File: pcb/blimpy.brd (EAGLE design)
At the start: 250 x 167 mm, 76 parts, among them J1 MICRO-USB, J4 3-PIN SMD, J5 3-PIN SMD, J6 3-PIN SMD, J7 3-PIN SMD, Q1 mmbt2222, Q2 mmbt2222, Q3 DMG3415U, U1 RGB, U10 MAX17048, U2 AP2112-3.3, U3 MCP73831T-2, U4 BNO080, U5 SX1509, U6 SX1509, U7 CP2104, U9 ESP-WROOM-32

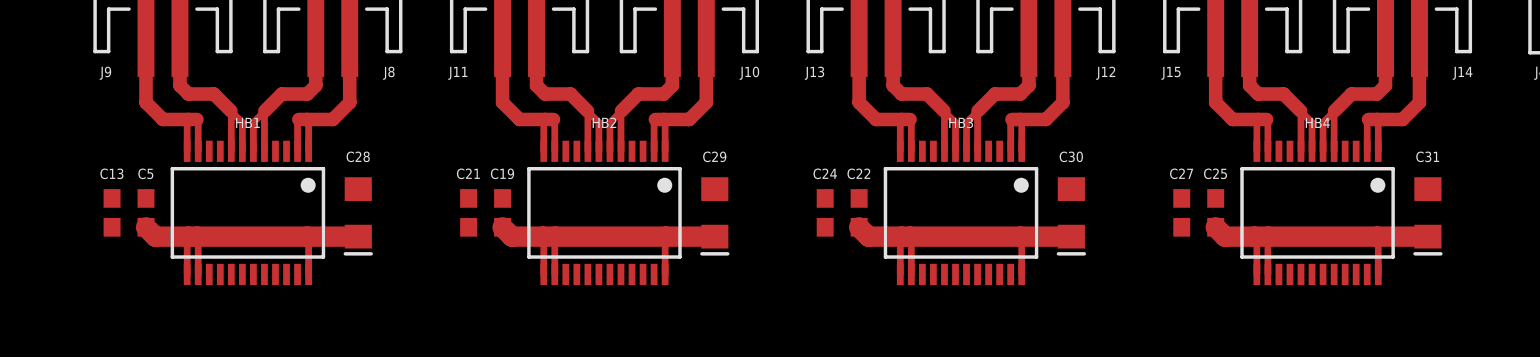
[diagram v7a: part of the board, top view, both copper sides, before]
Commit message: added hbridge gnd  traces
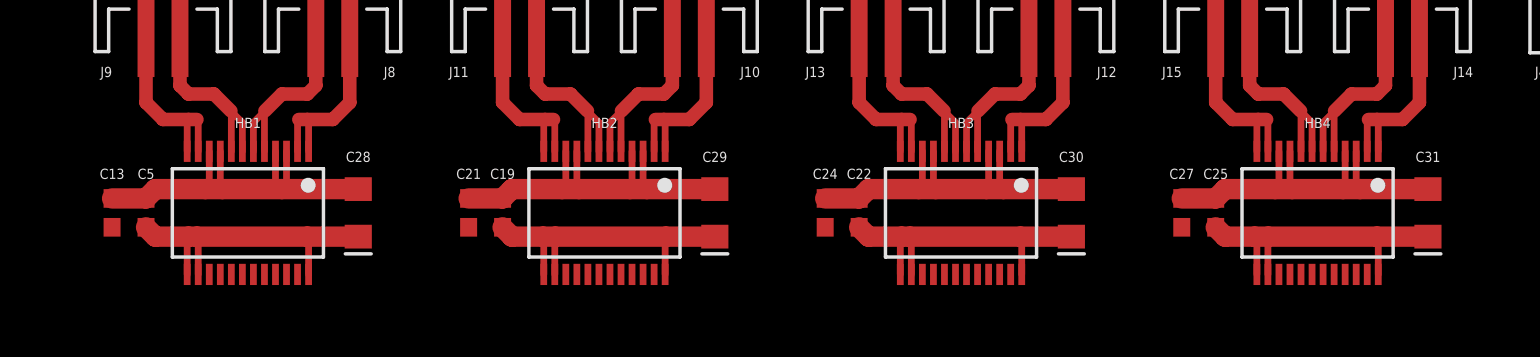
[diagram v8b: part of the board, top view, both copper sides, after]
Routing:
- net GND: track 0.00 -> 95.8 mm
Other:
- board text added: "Trace Widths for 1oz Copper: Logic: 0.4mm, 15mil (1A) Actors: 0.8mm, 30mil (2A) HBridge: 1.2mm, 45mil (3A) Battery: 1.6mm, 60mil (4A) Text Sizes Vector, 0.6, 15%"
- board text removed: "Trace Widths for 1oz Copper: Logic: 0.4mm, 15mil Actors: 0.8mm, 30mil (2A) Battery: 1.6mm, 60mil (4A) Text Sizes Vector, 0.6, 15%"
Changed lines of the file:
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@@
 <text x="225" y="75.5" size="0.6" layer="25" font="vector" ratio="15" align="bottom-center">U1</text>
 <text x="7" y="170.5" size="1.778" layer="51">Trace Widths for 1oz Copper:
-Logic: 0.4mm, 15mil
+Logic: 0.4mm, 15mil (1A)
 Actors: 0.8mm, 30mil (2A)
+HBridge: 1.2mm, 45mil (3A)
 Battery: 1.6mm, 60mil (4A)
 Text Sizes
@@
 <contactref element="U10" pad="P$9"/>
 <contactref element="C11" pad="2"/>
-<wire x1="106.125" y1="147.125" x2="106.775" y2="147.125" width="0" layer="19" extent="1-1"/>
-<wire x1="102.875" y1="147.125" x2="106.125" y2="147.125" width="0" layer="19" extent="1-1"/>
-<wire x1="102.225" y1="147.125" x2="102.875" y2="147.125" width="0" layer="19" extent="1-1"/>
-<wire x1="98.5" y1="144.35" x2="102.225" y2="147.125" width="0" layer="19" extent="1-1"/>
-<wire x1="96.5" y1="144.35" x2="98.5" y2="144.35" width="0" layer="19" extent="1-1"/>
-<wire x1="111" y1="144.9" x2="106.775" y2="147.125" width="0" layer="19" extent="1-1"/>
+<wire x1="48" y1="144.9" x2="43.5" y2="144.9" width="1.2" layer="1"/>
+<wire x1="43.5" y1="144.9" x2="40" y2="144.9" width="1.2" layer="1"/>
+<wire x1="40" y1="144.9" x2="39" y2="144.9" width="1.2" layer="1"/>
+<wire x1="39" y1="144.9" x2="36.05" y2="144.9" width="1.2" layer="1"/>
+<wire x1="36.05" y1="144.9" x2="35.5" y2="144.35" width="1.2" layer="1"/>
+<wire x1="33.5" y1="144.35" x2="35.5" y2="144.35" width="1.2" layer="1"/>
+<wire x1="69" y1="144.9" x2="65" y2="144.9" width="1.2" layer="1"/>
+<wire x1="65" y1="144.9" x2="64" y2="144.9" width="1.2" layer="1"/>
+<wire x1="64" y1="144.9" x2="61" y2="144.9" width="1.2" layer="1"/>
+<wire x1="61" y1="144.9" x2="60" y2="144.9" width="1.2" layer="1"/>
+<wire x1="60" y1="144.9" x2="57.05" y2="144.9" width="1.2" layer="1"/>
+<wire x1="57.05" y1="144.9" x2="56.5" y2="144.35" width="1.2" layer="1"/>
+<wire x1="56.5" y1="144.35" x2="54.5" y2="144.35" width="1.2" layer="1"/>
+<wire x1="90" y1="144.9" x2="86" y2="144.9" width="1.2" layer="1"/>
+<wire x1="86" y1="144.9" x2="85" y2="144.9" width="1.2" layer="1"/>
+<wire x1="85" y1="144.9" x2="82" y2="144.9" width="1.2" layer="1"/>
+<wire x1="82" y1="144.9" x2="81" y2="144.9" width="1.2" layer="1"/>
+<wire x1="81" y1="144.9" x2="78.05" y2="144.9" width="1.2" layer="1"/>
+<wire x1="78.05" y1="144.9" x2="77.5" y2="144.35" width="1.2" layer="1"/>
+<wire x1="77.5" y1="144.35" x2="75.5" y2="144.35" width="1.2" layer="1"/>
+<wire x1="111" y1="144.9" x2="107" y2="144.9" width="1.2" layer="1"/>
+<wire x1="107" y1="144.9" x2="106" y2="144.9" width="1.2" layer="1"/>
+<wire x1="106" y1="144.9" x2="103" y2="144.9" width="1.2" layer="1"/>
+<wire x1="103" y1="144.9" x2="102" y2="144.9" width="1.2" layer="1"/>
+<wire x1="102" y1="144.9" x2="99.05" y2="144.9" width="1.2" layer="1"/>
+<wire x1="99.05" y1="144.9" x2="98.5" y2="144.35" width="1.2" layer="1"/>
+<wire x1="98.5" y1="144.35" x2="96.5" y2="144.35" width="1.2" layer="1"/>
+<wire x1="106.775" y1="147.125" x2="106.775" y2="145.125" width="0.4" layer="1"/>
+<wire x1="106.775" y1="145.125" x2="107" y2="144.9" width="0.4" layer="1"/>
+<wire x1="106.125" y1="147.125" x2="106.125" y2="145.025" width="0.4" layer="1"/>
+<wire x1="106.125" y1="145.025" x2="106" y2="144.9" width="0.4" layer="1"/>
+<wire x1="102.875" y1="147.125" x2="102.875" y2="145.025" width="0.4" layer="1"/>
+<wire x1="102.875" y1="145.025" x2="103" y2="144.9" width="0.4" layer="1"/>
+<wire x1="102.225" y1="147.125" x2="102.225" y2="145.125" width="0.4" layer="1"/>
+<wire x1="102.225" y1="145.125" x2="102" y2="144.9" width="0.4" layer="1"/>
+<wire x1="85.125" y1="147.125" x2="85.125" y2="145.025" width="0.4" layer="1"/>
+<wire x1="85.125" y1="145.025" x2="85" y2="144.9" width="0.4" layer="1"/>
+<wire x1="85.775" y1="147.125" x2="85.775" y2="145.125" width="0.4" layer="1"/>
+<wire x1="85.775" y1="145.125" x2="86" y2="144.9" width="0.4" layer="1"/>
+<wire x1="81.875" y1="147.125" x2="81.875" y2="145.025" width="0.4" layer="1"/>
+<wire x1="81.875" y1="145.025" x2="82" y2="144.9" width="0.4" layer="1"/>
+<wire x1="81.225" y1="147.125" x2="81.225" y2="145.125" width="0.4" layer="1"/>
+<wire x1="81.225" y1="145.125" x2="81" y2="144.9" width="0.4" layer="1"/>
+<wire x1="64.775" y1="147.125" x2="64.775" y2="145.125" width="0.4" layer="1"/>
+<wire x1="64.775" y1="145.125" x2="65" y2="144.9" width="0.4" layer="1"/>
+<wire x1="64.125" y1="147.125" x2="64.125" y2="145.025" width="0.4" layer="1"/>
+<wire x1="64.125" y1="145.025" x2="64" y2="144.9" width="0.4" layer="1"/>
+<wire x1="60.875" y1="147.125" x2="60.875" y2="145.025" width="0.4" layer="1"/>
+<wire x1="60.875" y1="145.025" x2="61" y2="144.9" width="0.4" layer="1"/>
+<wire x1="60.225" y1="147.125" x2="60.225" y2="145.125" width="0.4" layer="1"/>
+<wire x1="60.225" y1="145.125" x2="60" y2="144.9" width="0.4" layer="1"/>
+<wire x1="43.775" y1="147.125" x2="43.775" y2="145.175" width="0.4" layer="1"/>
+<wire x1="43.775" y1="145.175" x2="43.5" y2="144.9" width="0.4" layer="1"/>
+<wire x1="43.125" y1="147.125" x2="43.125" y2="145.275" width="0.4" layer="1"/>
+<wire x1="43.125" y1="145.275" x2="43.5" y2="144.9" width="0.4" layer="1"/>
+<wire x1="39.875" y1="147.125" x2="39.875" y2="145.025" width="0.4" layer="1"/>
+<wire x1="39.875" y1="145.025" x2="40" y2="144.9" width="0.4" layer="1"/>
+<wire x1="39.225" y1="147.125" x2="39.225" y2="145.125" width="0.4" layer="1"/>
+<wire x1="39.225" y1="145.125" x2="39" y2="144.9" width="0.4" layer="1"/>
+<wire x1="98.5" y1="144.35" x2="104.175" y2="139.875" width="0" layer="19" extent="1-1"/>
 <wire x1="90" y1="144.9" x2="96.5" y2="144.35" width="0" layer="19" extent="1-1"/>
-<wire x1="85.775" y1="147.125" x2="90" y2="144.9" width="0" layer="19" extent="1-1"/>
-<wire x1="85.125" y1="147.125" x2="85.775" y2="147.125" width="0" layer="19" extent="1-1"/>
-<wire x1="81.875" y1="147.125" x2="85.125" y2="147.125" width="0" layer="19" extent="1-1"/>
-<wire x1="81.225" y1="147.125" x2="81.875" y2="147.125" width="0" layer="19" extent="1-1"/>
-<wire x1="77.5" y1="144.35" x2="81.225" y2="147.125" width="0" layer="19" extent="1-1"/>
-<wire x1="75.5" y1="144.35" x2="77.5" y2="144.35" width="0" layer="19" extent="1-1"/>
 <wire x1="69" y1="144.9" x2="75.5" y2="144.35" width="0" layer="19" extent="1-1"/>
-<wire x1="64.775" y1="147.125" x2="69" y2="144.9" width="0" layer="19" extent="1-1"/>
-<wire x1="64.125" y1="147.125" x2="64.775" y2="147.125" width="0" layer="19" extent="1-1"/>
-<wire x1="60.875" y1="147.125" x2="64.125" y2="147.125" width="0" layer="19" extent="1-1"/>
-<wire x1="60.225" y1="147.125" x2="60.875" y2="147.125" width="0" layer="19" extent="1-1"/>
-<wire x1="56.5" y1="144.35" x2="60.225" y2="147.125" width="0" layer="19" extent="1-1"/>
-<wire x1="54.5" y1="144.35" x2="56.5" y2="144.35" width="0" layer="19" extent="1-1"/>
 <wire x1="48" y1="144.9" x2="54.5" y2="144.35" width="0" layer="19" extent="1-1"/>
-<wire x1="43.775" y1="147.125" x2="48" y2="144.9" width="0" layer="19" extent="1-1"/>
-<wire x1="43.125" y1="147.125" x2="43.775" y2="147.125" width="0" layer="19" extent="1-1"/>
-<wire x1="39.875" y1="147.125" x2="43.125" y2="147.125" width="0" layer="19" extent="1-1"/>
-<wire x1="39.225" y1="147.125" x2="39.875" y2="147.125" width="0" layer="19" extent="1-1"/>
-<wire x1="35.5" y1="144.35" x2="39.225" y2="147.125" width="0" layer="19" extent="1-1"/>
-<wire x1="33.5" y1="144.35" x2="35.5" y2="144.35" width="0" layer="19" extent="1-1"/>
-<wire x1="104.175" y1="139.875" x2="98.5" y2="144.35" width="0" layer="19" extent="1-1"/>
 <wire x1="83.175" y1="139.875" x2="77.5" y2="144.35" width="0" layer="19" extent="1-1"/>
 <wire x1="62.175" y1="139.875" x2="56.5" y2="144.35" width="0" layer="19" extent="1-1"/>
